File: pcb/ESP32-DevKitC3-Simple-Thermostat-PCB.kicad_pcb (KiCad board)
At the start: 4 copper layers, 133 x 89.5 mm, 61 parts, among them J1 PINHD_1x18_Male, J2 Screw_Terminal_9_P3.50mm, J3 DS18B20, J4 3.2 lcd tft, J5 I2C Sensor, J6 LD2410C, J7 PINHD_1x3_Male, K1 G5Q-1A, K2 G5Q-1A, K3 G5Q-1A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

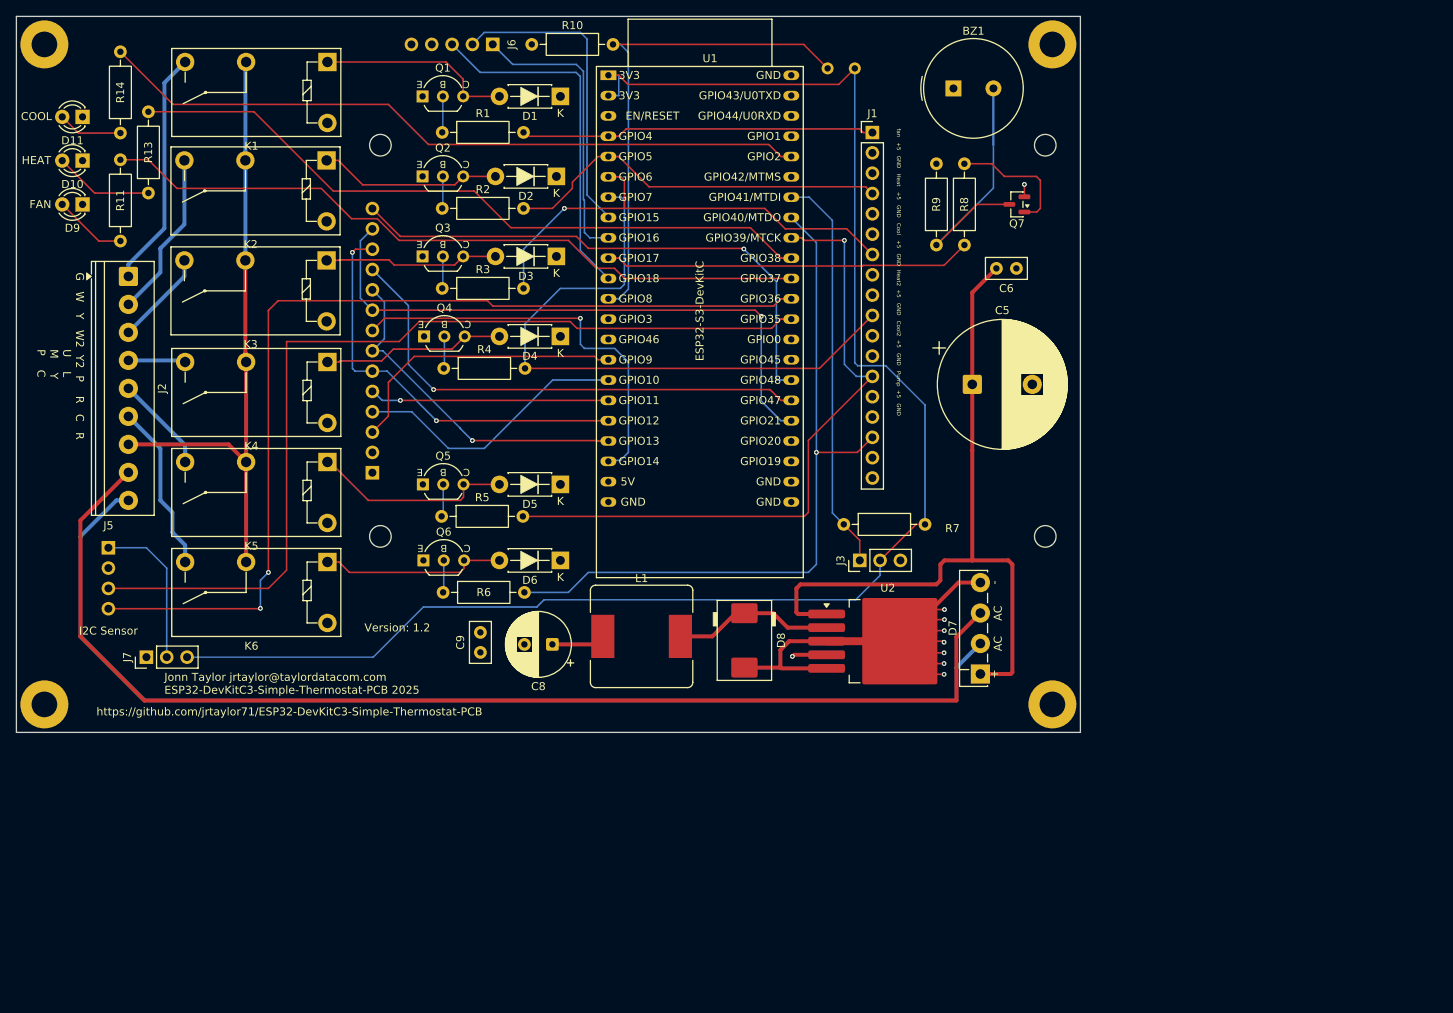
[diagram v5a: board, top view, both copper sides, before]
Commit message: Update PCB and remove extra 3.3v netlist.
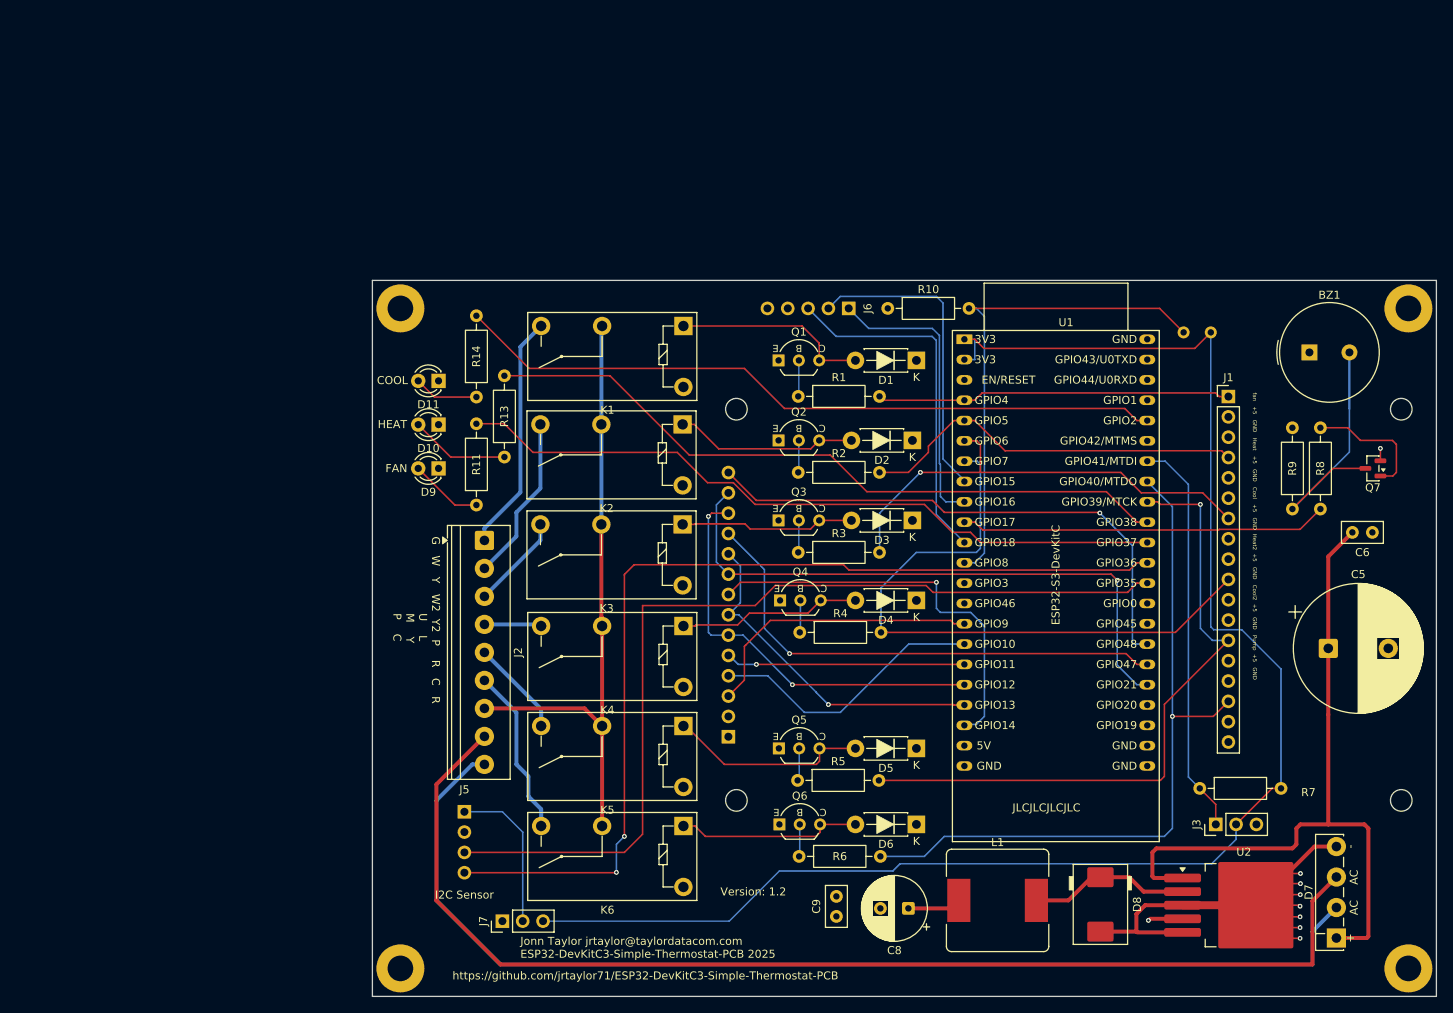
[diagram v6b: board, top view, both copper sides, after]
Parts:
- R12: value LDR07 -> GL5537
- moved R12 55.4 mm to (170.8, 67.5)
- moved BZ1 55.4 mm to (183.1, 70.0)
- moved C5 55.4 mm to (185.5, 107.0)
- moved C6 55.4 mm to (191.0, 92.5)
- moved C8 55.4 mm to (133.0, 139.5)
- moved C9 55.4 mm to (124.0, 140.5)
- moved D1 55.4 mm to (134.0, 71.0)
- moved D10 55.4 mm to (74.3, 79.0)
- moved D11 55.4 mm to (74.3, 73.6)
- moved D2 55.4 mm to (133.5, 81.0)
- moved D3 55.4 mm to (133.5, 91.0)
- moved D4 55.4 mm to (134.0, 101.0)
- moved D5 55.4 mm to (134.0, 119.5)
- moved D6 55.4 mm to (134.0, 129.0)
- moved D8 55.4 mm to (157.0, 139.0)
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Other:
- board text added: "JLCJLCJLCJLC"
